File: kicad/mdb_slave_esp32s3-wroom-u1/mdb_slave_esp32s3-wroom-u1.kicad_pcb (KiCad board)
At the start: 2 copper layers, 189.4 x 672.8 mm, 60 parts, among them J1 USB_C_Receptacle_USB2.0_16P, J10 Conn_01x04_Pin_JST, J11 Screw_Terminal_01x03, J12 MDB_Connector, J13 Screw_Terminal_01x03, J14 Screw_Terminal_01x03, J2 Screw_Terminal_01x02, J3 Screw_Terminal_01x02, J4 Screw_Terminal_01x03, J5 Screw_Terminal_01x03, J6 Screw_Terminal_01x03, J7 Conn_01x06_Pin, J8 Conn_01x03_Pin_JST, J9 Conn_01x04_Pin, Q1 MMBT3904, Q2 MMBT3904, Q3 MMBT3904, SW1 SW_Push, U1 ESP32-S3-WROOM-1U-N16R2, U2 AP63203QWU-7, U3 TLP785, U4 TLP785

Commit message: Update footprint and symbol for BUZZER + ESP32S3-WROOM-U1. PCB empty with all component on side.
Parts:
- removed BZ1: Buzzer, fasteda:BUZ-TH_BD23.0-P15.00-D0.8-FD
- added BUZZER1: MLT-8530, easyeda2kicad:BUZ-SMD_4P-L8.5-W8.5-P8.50-BR, F.Cu at (111.8, 28.4)
- added H1: MountingHole2.5, MountingHole:MountingHole_2.5mm, F.Cu at (309.0, 100.6)
- added H2: MountingHole2.5, MountingHole:MountingHole_2.5mm, F.Cu at (325.5, 112.1)
- added H3: MountingHole2.5, MountingHole:MountingHole_2.5mm, F.Cu at (346.0, 115.6)
- added H4: MountingHole2.5, MountingHole:MountingHole_2.5mm, F.Cu at (324.0, 99.1)
- added H5: MountingHole2.5, MountingHole:MountingHole_2.5mm, F.Cu at (346.0, 101.1)
- C1, C2: footprint fasteda:LED0603-RD -> Capacitor_SMD:C_0603_1608Metric
- C3, C4, C5, C6: footprint ProtoFlow_Auto:PinHeader_1x2 -> Capacitor_SMD:C_0603_1608Metric
- D1: footprint fasteda:DO-41_BD2.4-L4.7-P8.70-D0.9-RD -> Diode_SMD:D_SOD-123
- D2: footprint ProtoFlow_Auto:PinHeader_1x4 -> LED_SMD:LED_WS2812B-2020_PLCC4_2.0x2.0mm
- D3, D4: footprint fasteda:DFN1006-2L-RD -> Diode_SMD:D_SOD-123
- D5, D6: footprint fasteda:SOD-323_L1.8-W1.3-LS2.5-RD -> Diode_SMD:D_SOD-323
- F1: footprint ProtoFlow_Auto:PinHeader_1x2 -> Fuse:Fuse_1812_4532Metric
- J1: footprint ProtoFlow_Auto:PinHeader_1x11 -> Connector_USB:USB_C_Receptacle_G-Switch_GT-USB-7010ASV
- J10: footprint CONN-TH_B4B-PH-K-S -> Connector_JST:JST_PH_B4B-PH-K_1x04_P2.00mm_Vertical
- J11, J13, J14, J4, J5, J6: footprint ProtoFlow_Auto:PinHeader_1x3 -> EasyEDA2Kicad:CONN-TH_3P-P2.54_DIBO_DB141R-2.54-3P
- J12: footprint ProtoFlow_Auto:PinHeader_1x6 -> Connector_Molex:Molex_Mini-Fit_Jr_5566-06A_2x03_P4.20mm_Vertical
- J2, J3: footprint ProtoFlow_Auto:PinHeader_1x2 -> EasyEDA2Kicad:CONN-TH_2P-P2.54_DIBO_DB141R-2.54-2P
- J7: footprint ProtoFlow_Auto:PinHeader_1x6 -> Connector_PinHeader_2.54mm:PinHeader_1x06_P2.54mm_Vertical
- J8: footprint ProtoFlow_Auto:PinHeader_1x3 -> Connector_JST:JST_PH_B3B-PH-K_1x03_P2.00mm_Vertical
- J9: footprint ProtoFlow_Auto:PinHeader_1x4 -> Connector_PinHeader_2.54mm:PinHeader_1x04_P2.54mm_Vertical
- L1: footprint fasteda:LED0603-RD -> Inductor_SMD:L_TechFuse_SL0420
- Q1, Q2, Q3: footprint fasteda:SOT-23-3_L2.9-W1.3-P1.90-LS2.4-BR -> Package_TO_SOT_SMD:SOT-23
- R1, R10, R11, R12, R13, R14, R15, R16, R17, R18, R19, R2, R20, R21, R22, R3, R4, R5, R6, R7, R8, R9: footprint fasteda:LED0603-RD -> Resistor_SMD:R_0603_1608Metric
- SW1: footprint ProtoFlow_Auto:PinHeader_1x2 -> Button_Switch_SMD:SW_Tactile_SPST_NO_Straight_CK_PTS636Sx25SMTRLFS
- TH1: footprint ProtoFlow_Auto:PinHeader_1x2 -> Resistor_SMD:R_0603_1608Metric
- U1: footprint fasteda:WIRELM-SMD_ESP32-S3-WROOM-1U -> RF_Module:ESP32-S3-WROOM-1U
- U2: footprint fasteda:TSOT-26_L2.9-W1.6-P0.95-LS2.8-BL -> Package_TO_SOT_SMD:TSOT-23-6
- U3, U4: footprint fasteda:DIP-4_L6.4-W4.6-P2.54-LS7.6-BL -> Package_DIP:DIP-4_W7.62mm
- moved D2 600.2 mm to (223.9, 83.0)
- moved TH1 594.0 mm to (66.0, 67.3), turned to 90 degrees
- moved R7 578.3 mm to (84.7, 82.6), turned to 0 degrees
- moved C2 556.2 mm to (76.7, 47.6), turned to 0 degrees
- moved C6 472.6 mm to (101.2, 46.1)
- moved J1 472.5 mm to (156.0, 29.1)
- moved C5 466.1 mm to (96.2, 44.6)
- moved D1 456.3 mm to (213.0, 78.6), turned to 0 degrees
- moved C4 453.2 mm to (90.0, 45.1), turned to 0 degrees
- moved C3 437.5 mm to (83.7, 45.1), turned to 0 degrees
- moved L1 434.3 mm to (169.2, 84.1), turned to 0 degrees
- moved U2 431.8 mm to (146.9, 79.1), turned to 0 degrees
- moved R4 388.2 mm to (81.0, 95.1), turned to 0 degrees
- moved R3 386.1 mm to (74.0, 95.1)
- moved J7 352.0 mm to (131.5, 33.4)
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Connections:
- net N_0BA757E2 renamed Net-(U1-IO46)
- net N_1C04F8A7 renamed Net-(J8-Pin_3)
- net N_23AED94E renamed Net-(U1-EN)
- net N_47FE5074 renamed Net-(D6-A)
- net N_4E7C1FC4 renamed Net-(U1-IO45)
- net N_6D558B4C renamed Net-(D5-A)
- net N_7E66AFB6 renamed Net-(U2-BST)
- net N_7EFCD247 renamed Net-(J1-CC2)
- net N_82420577 renamed Net-(J1-CC1)
- net N_839742D6 renamed Net-(D6-K)
- net N_8CE5999C renamed Net-(J12-Pin_1)
- net N_8FD5F3B3 renamed Net-(Q3-B)
- net N_ACA98A90 renamed Net-(D5-K)
- net N_B32CF7B9 renamed Net-(Q2-B)
- net N_E2031F96 renamed Net-(Q1-B)
- net N_E272A5AA renamed Net-(U2-SW)
- net io1 renamed /io1
- net io12 renamed /io12
- net io13 renamed /io13
- net io2 renamed /io2
- net io21 renamed /io21
- net io39 renamed /io39
- net io4 renamed /io4
- net io40 renamed /io40
- net io41 renamed /io41
- net io42 renamed /io42
- net io5 renamed /io5
- net mdb_communications_common renamed /mdb_communications_common
- net mdb_master_receive renamed /mdb_master_receive
- net mdb_master_transmit renamed /mdb_master_transmit
- net u0rxd renamed /u0rxd
- net u0txd renamed /u0txd
- net usb+ renamed /usb+
- net usb- renamed /usb-
- C3 pad 1: N_77AE7822 -> /vin
- C3 pad 2: vin -> Net-(U2-IN)
- D1 pad 1: vin -> /vin
- D1 pad 2: N_37949F46 -> Net-(D1-A)
- D2 pad 1: N_1B3C62E2 -> unconnected-(D2-DOUT-Pad1)
- D3 pad 1: N_B7B926F7 -> +3V3
- D3 pad 2: +3V3 -> Net-(D3-A)
- D4 pad 1: N_28FD65AA -> +3V3
- D4 pad 2: +3V3 -> Net-(D4-A)
- F1 pad 1: vin -> /vin
- J1 pad A4: N_37949F46 -> Net-(D1-A)
- J1 pad A8: N_01021B2F -> unconnected-(J1-SBU1-PadA8)
- J1 pad B8: N_7EFA92C4 -> unconnected-(J1-SBU2-PadB8)
- J10 pad 3: N_FD44900F -> /io10
- J10 pad 4: N_4EC59133 -> /io11
- J11 pad 3: io6 -> /io6
- J12 pad 3: N_95D6C915 -> unconnected-(J12-Pin_3-Pad3)
- J13 pad 3: io8 -> /io8
- J14 pad 3: io9 -> /io9
- J2 pad 1: N_B7B926F7 -> Net-(D3-A)
- J3 pad 1: N_28FD65AA -> Net-(D4-A)
- J4 pad 3: io15 -> /io15
- J5 pad 3: io15 -> /io15
- J6 pad 3: io16 -> /io16
- J8 pad 2: vin -> /vin
- Q1 pad 3: N_B7B926F7 -> Net-(D3-A)
- Q2 pad 3: N_28FD65AA -> Net-(D4-A)
- R1 pad 1: +3V3 -> /boot
- R1 pad 2: boot -> +3V3
- R11 pad 1: io15 -> +3V3
- R11 pad 2: +3V3 -> /io15
- R12 pad 1: N_343FCC35 -> Net-(BUZZER1-+)
- R13 pad 1: +3V3 -> /io16
- R13 pad 2: io16 -> +3V3
- R15 pad 1: N_4EC59133 -> /io11
- R16 pad 1: N_FD44900F -> /io10
- R17 pad 1: +3V3 -> /io6
- R17 pad 2: io6 -> +3V3
- R19 pad 1: +3V3 -> /io8
- R19 pad 2: io8 -> +3V3
- R22 pad 1: +3V3 -> /io9
- R22 pad 2: io9 -> +3V3
- R7 pad 1: N_7F4ACBB8 -> /io7
- R8 pad 1: +3V3 -> /io15
- R8 pad 2: io15 -> +3V3
- SW1 pad 1: boot -> /boot
- TH1 pad 2: N_7F4ACBB8 -> /io7
- U1 pad 10: N_359D8FB6 -> unconnected-(U1-IO17-Pad10)
- U1 pad 11: N_369D9149 -> unconnected-(U1-IO18-Pad11)
- U1 pad 12: io8 -> /io8
- U1 pad 15: N_3A9D9795 -> unconnected-(U1-IO3-Pad15)
- U1 pad 17: io9 -> /io9
- U1 pad 18: io10 -> /io10
- U1 pad 19: io11 -> /io11
- U1 pad 22: N_CD9AAD67 -> unconnected-(U1-IO14-Pad22)
- U1 pad 24: N_CB9AAA41 -> unconnected-(U1-IO47-Pad24)
- U1 pad 25: N_CA9AA8AE -> unconnected-(U1-IO48-Pad25)
- U1 pad 27: boot -> /boot
- U1 pad 28: N_C79AA3F5 -> unconnected-(U1-IO35-Pad28)
- U1 pad 29: N_C69AA262 -> unconnected-(U1-IO36-Pad29)
- U1 pad 30: N_C9986884 -> unconnected-(U1-IO37-Pad30)
- U1 pad 31: N_CA986A17 -> unconnected-(U1-IO38-Pad31)
- U1 pad 40: (no net) -> GND
- U1 pad 41: (no net) -> GND
- U1 pad 6: io6 -> /io6
- U1 pad 7: io7 -> /io7
- U1 pad 8: io15 -> /io15
- U1 pad 9: io16 -> /io16
- U2 pad 2: vin -> /vin
- U2 pad 3: N_77AE7822 -> Net-(U2-IN)
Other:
- board size 189.4 x 672.8 mm -> 135 x 65 mm
- board text added: "VMflow"
- board text added: "commit xxxxxxx"
- board text added: "github.com/lucienkerl/mdb-esp32-cashless"
- board text added: "mdb-slave-esp32s3-wroom-u1"

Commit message: Move custom_input2/3 from IO8/IO9 to IO47/IO48
IO8/IO9 collided with PIN_DEX_RX/PIN_DEX_TX on the original
mdb-slave-esp32s3 board, so flashing the wrong firmware onto either
board would silently misdrive these pins instead of erroring.

IO17/IO18 were considered as an alternative but rejected — those
collide with PIN_SIM7080G_TX/RX on the basic-plus/cellular variant
instead, trading one cross-board conflict for another.

IO47/IO48 are free on every board variant and unaffected by
Quad-vs-Octal PSRAM pin reservations (unlike IO35-37), so J13/J14 and
their pull-up resistors are rerouted there. IO8/IO9 are now
no-connect.

Firmware side already updated on feature/esp32s3-wroom-u1-firmware
(PIN_CUSTOM_INPUT1/2/3 defines).
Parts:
- moved J12 154.2 mm to (173.1, 127.6)
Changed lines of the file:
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@@
 	(footprint "Connector_Molex:Molex_Mini-Fit_Jr_5566-06A_2x03_P4.20mm_Vertical"
 		(layer "F.Cu")
-		(at 51.61 32.58)
+		(at 173.11 127.58)
 		(descr "Molex Mini-Fit Jr. Power Connectors, old mpn/engineering number: 5566-06A, example for new mpn: 39-28-x06x, 3 Pins per row, Mounting:  (http://www.molex.com/pdm_docs/sd/039281043_sd.pdf)")
 		(tags "connector Molex Mini-Fit_Jr vertical")

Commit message: fix(hardware): add GPIO3 pull-down strap for WROOM-U1 board detection
Add a 10kΩ pull-down resistor from GPIO3 (pin 15 on the ESP32-S3-WROOM-1
symbol) to GND. This was previously unconnected on this board revision.
Lets detect_board_variant() read GPIO3 LOW at boot and correctly identify
the WROOM-U1 board, so DEX/UART1 init is skipped as intended (matches the
firmware-side README in mdb-slave-esp32s3-wroom-u1).
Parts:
- added R23: 10k, Resistor_SMD:R_0603_1608Metric, F.Cu at (67.5, 31.8)
- U1: footprint RF_Module:ESP32-S3-WROOM-1U -> EasyEDA2Kicad:WIRELM-SMD_ESP32-S3-WROOM-1U
- U3, U4: footprint Package_DIP:DIP-4_W7.62mm -> EasyEDA2Kicad:SMD-4_L4.6-W3.7-P2.54-LS7.0-BR
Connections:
- J13 pad 3: /io8 -> /io47
- J14 pad 3: /io9 -> /io48
- R19 pad 1: /io8 -> /io47
- R22 pad 1: /io9 -> /io48
- U1 pad 12: /io8 -> unconnected-(U1-IO8-Pad12)
- U1 pad 15: unconnected-(U1-IO3-Pad15) -> Net-(U1-IO3)
- U1 pad 17: /io9 -> unconnected-(U1-IO9-Pad17)
- U1 pad 24: unconnected-(U1-IO47-Pad24) -> /io47
- U1 pad 25: unconnected-(U1-IO48-Pad25) -> /io48

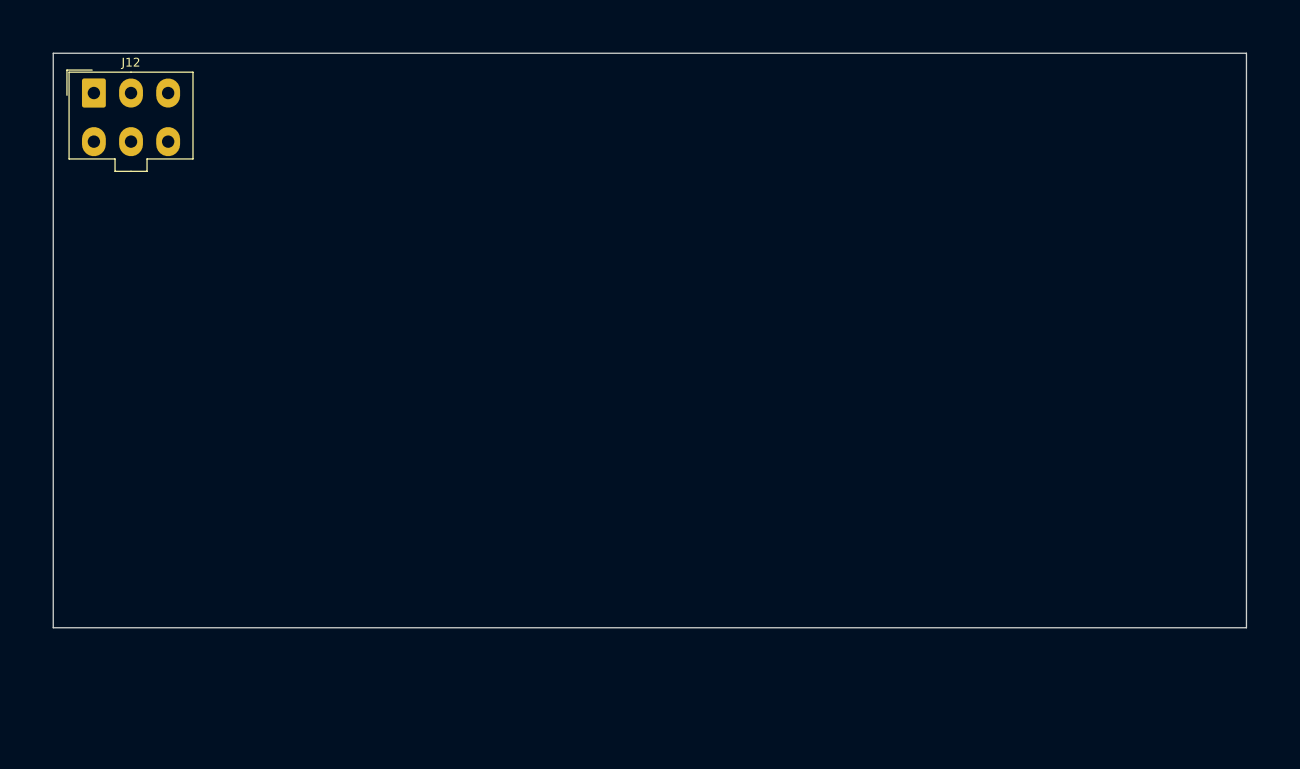
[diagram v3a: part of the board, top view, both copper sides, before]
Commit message: Update missing footprint and LCSC components ref.
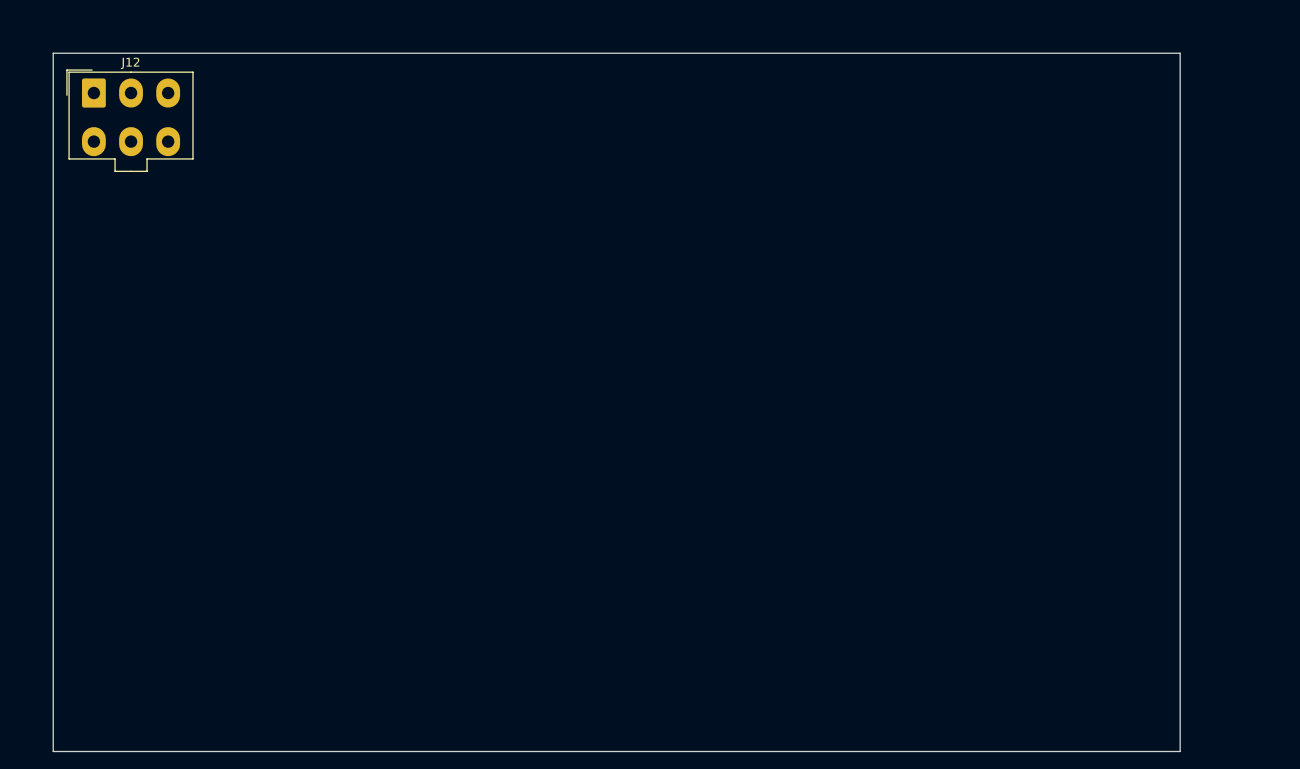
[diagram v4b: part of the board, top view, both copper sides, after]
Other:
- board size 135 x 65 mm -> 127.5 x 79 mm
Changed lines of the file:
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@@
 	(gr_rect
 		(start 168.51 123.08)
-		(end 303.51 188.08)
+		(end 296.01 202.08)
 		(stroke
 			(width 0.05)
